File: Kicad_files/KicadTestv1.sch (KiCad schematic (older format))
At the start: 7 parts, among them J1 Conn_01x10_MountingPin, J2 Conn_01x04, SW1 SW_Push

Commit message: Ajout Lib pour RN2483 & Modificition Empreinte et cablage
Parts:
- removed J1: Conn_01x10_MountingPin, Connector_PinHeader_2.00mm:PinHeader_1x10_P2.00mm_Vertical, symbol Connector_Generic_MountingPin:Conn_01x10_MountingPin
- added U1: RN2483A, Socket_Arduino_Uno:Socket_Strip_Arduino_1x08, symbol Shield_Arduino:RN2483A
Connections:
- net labels added: +3V3
- wire segments 29 -> 34
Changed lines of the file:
@@
 	3450 2450 3450 2550
-$Comp
-L Connector_Generic_MountingPin:Conn_01x10_MountingPin J1
-U 1 1 5DDC7E9D
-P 5750 3800
-F 0 "J1" H 5838 3714 50  0000 L CNN
-F 1 "Conn_01x10_MountingPin" H 5838 3623 50  0000 L CNN
-F 2 "Connector_PinHeader_2.00mm:PinHeader_1x10_P2.00mm_Vertical" H 5750 3800 50  0001 C CNN
-F 3 "~" H 5750 3800 50  0001 C CNN
-	1    5750 3800
-	1    0    0    -1
-$EndComp
 $Comp
 L Connector_Generic:Conn_01x04 J2
@@
 Text GLabel 5300 3500 0    50   Input ~ 0
 Rx
-Text GLabel 5300 4000 0    50   Input ~ 0
+Text GLabel 5300 3700 0    50   Input ~ 0
 RST
 Wire Wire Line
@@
 Wire Wire Line
 	5300 3500 5550 3500
-Wire Wire Line
-	5550 4000 5300 4000
 Text GLabel 2350 4200 0    50   Input ~ 0
 Tx
@@
 	3250 4950 3250 4800
 Wire Wire Line
-	4700 3150 4700 4300
-Wire Wire Line
-	4700 4300 5550 4300
-Wire Wire Line
-	4700 4950 4700 4300
-Connection ~ 4700 4300
-Wire Wire Line
-	4050 4200 4050 3050
-Wire Wire Line
 	4050 2550 3450 2550
-Wire Wire Line
-	4050 4200 5550 4200
 Connection ~ 3450 2550
 Wire Wire Line
@@
 Wire Wire Line
 	4050 3050 4900 3050
-Connection ~ 4050 3050
 $Comp
 L Switch:SW_Push SW1
@@
 Wire Wire Line
 	2750 4000 2350 4000
+$Comp
+L Shield_Arduino:RN2483A U1
+U 1 1 5DE7C31C
+P 5750 3750
+F 0 "U1" V 5704 3978 50  0000 L CNN
+F 1 "RN2483A" V 5795 3978 50  0000 L CNN
+F 2 "Socket_Arduino_Uno:Socket_Strip_Arduino_1x08" H 6100 3700 50  0001 C CNN
+F 3 "" H 6100 3700 50  0001 C CNN
+	1    5750 3750
+	0    1    1    0
+$EndComp
+Wire Wire Line
+	4700 3150 4700 4100
+Wire Wire Line
+	5550 4100 4700 4100
+Connection ~ 4700 4100
+Wire Wire Line
+	4700 4100 4700 4950
+Wire Wire Line
+	5550 3700 5300 3700
+$Comp
+L power:+3V3 #PWR0101
+U 1 1 5DE826CD
+P 3300 2450
+F 0 "#PWR0101" H 3300 2300 50  0001 C CNN
+F 1 "+3V3" H 3315 2623 50  0000 C CNN
+F 2 "" H 3300 2450 50  0001 C CNN
+F 3 "" H 3300 2450 50  0001 C CNN
+	1    3300 2450
+	1    0    0    -1
+$EndComp
+Wire Wire Line
+	3300 2450 3300 2700
+Wire Wire Line
+	3300 2700 3350 2700
+$Comp
+L power:+3V3 #PWR0102
+U 1 1 5DE833AF
+P 4950 3850
+F 0 "#PWR0102" H 4950 3700 50  0001 C CNN
+F 1 "+3V3" H 4965 4023 50  0000 C CNN
+F 2 "" H 4950 3850 50  0001 C CNN
+F 3 "" H 4950 3850 50  0001 C CNN
+	1    4950 3850
+	1    0    0    -1
+$EndComp
+Wire Wire Line
+	5550 3900 4950 3900
+Wire Wire Line
+	4950 3900 4950 3850
+Wire Wire Line
+	5550 4000 4950 4000
+Wire Wire Line
+	4950 4000 4950 3900
+Connection ~ 4950 3900
+Text GLabel 4050 3700 2    50   Input ~ 0
+A0
+Wire Wire Line
+	4050 3700 3750 3700
 $EndSCHEMATC

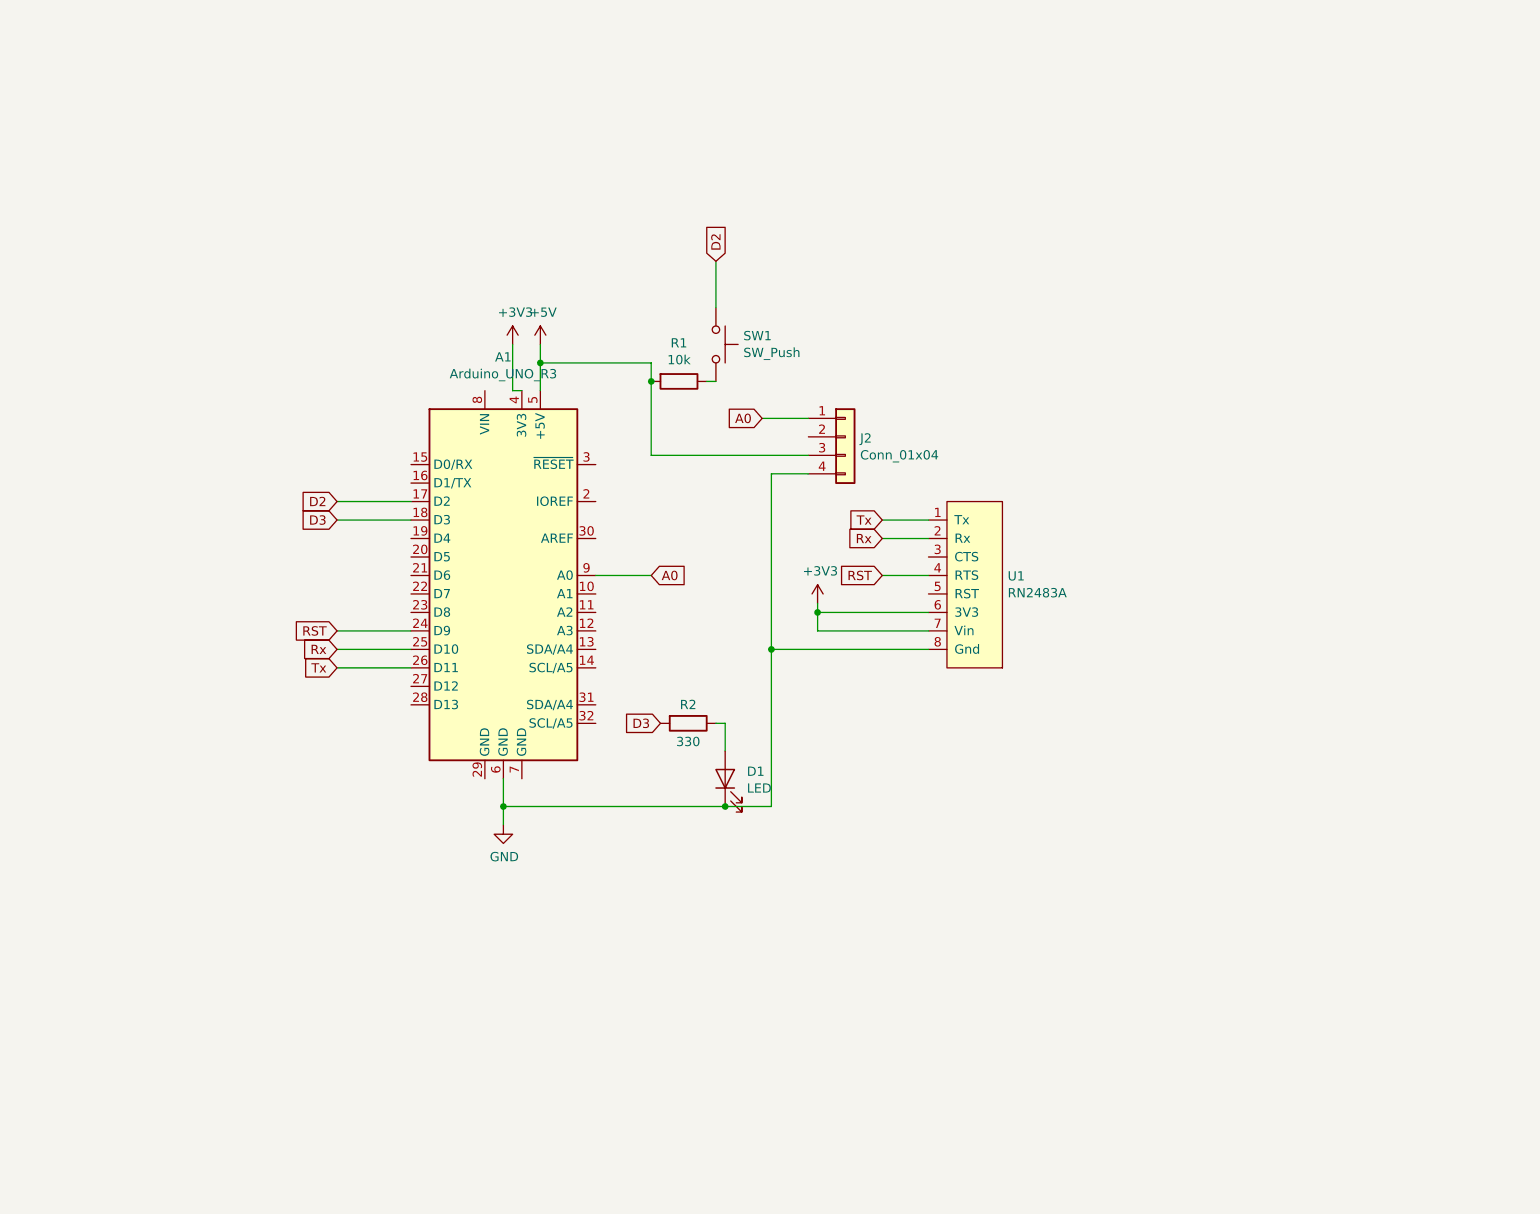
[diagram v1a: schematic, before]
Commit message: Modification empreinte et ajout circuit capteur AIME + faire routage
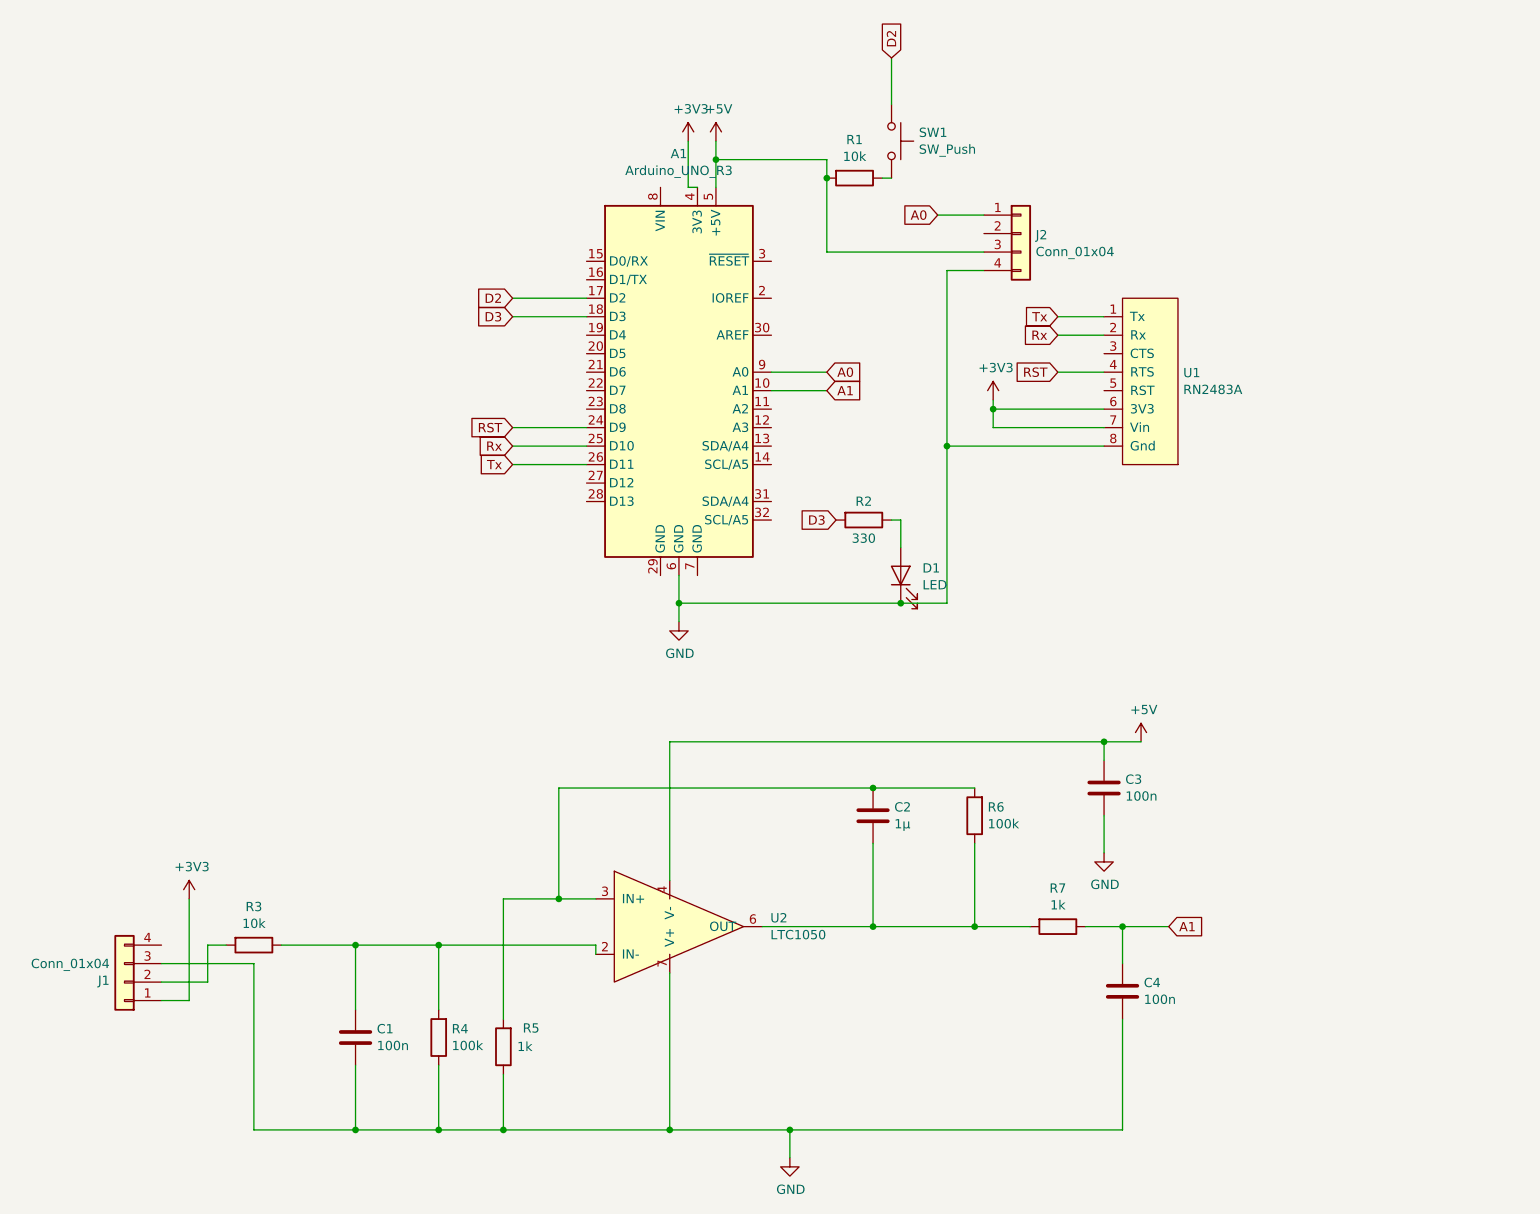
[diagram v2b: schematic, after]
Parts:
- added C1, C3, C4: 100n, Capacitor_THT:C_Axial_L3.8mm_D2.6mm_P7.50mm_Horizontal, symbol Device:C
- added C2: 1µ, Capacitor_THT:C_Rect_L7.0mm_W4.5mm_P5.00mm, symbol Device:C
- added J1: Conn_01x04, ShieldArduino_Empreintes:TO-5-4_1, symbol Connector_Generic:Conn_01x04
- added R3: 10k, Resistor_THT:R_Axial_DIN0204_L3.6mm_D1.6mm_P7.62mm_Horizontal, symbol Device:R
- added R4, R6: 100k, Resistor_THT:R_Axial_DIN0204_L3.6mm_D1.6mm_P7.62mm_Horizontal, symbol Device:R
- added R5, R7: 1k, Resistor_THT:R_Axial_DIN0204_L3.6mm_D1.6mm_P7.62mm_Horizontal, symbol Device:R
- added U2: LTC1050, symbol Shield_Arduino_suite:LTC1050
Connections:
- net +3V3: now also J1.1 (Pin_1)
- net +5V: now also C3.1, U2.4 (V-)
- net GND: now also C1.2, C3.2, C4.2, J1.3 (Pin_3), R4.1, R5.1, U2.7 (V+)
- net A1: now reaches A1.10 (A1)
- net A1: now also C4.1, R7.1
- new net: C2.2, R6.1, R7.2, U2.6 (OUT)
- new net: C1.1, R3.1, R4.2, U2.2 (IN-)
- new net: C2.1, R5.2, R6.2, U2.3 (IN+)
- new net: J1.2 (Pin_2), R3.2
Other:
- moved on the sheet: A1, D1, J2, R1, R2, SW1, U1

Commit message: Debut cablages
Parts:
- U2: footprint (none) -> Package_DIP:DIP-8_W7.62mm_LongPads
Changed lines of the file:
@@
 F 0 "U2" H 4694 5646 50  0000 L CNN
 F 1 "LTC1050" H 4694 5555 50  0000 L CNN
-F 2 "" H 4100 5600 50  0001 C CNN
+F 2 "Package_DIP:DIP-8_W7.62mm_LongPads" H 4100 5600 50  0001 C CNN
 F 3 "" H 4100 5600 50  0001 C CNN
 	1    4100 5600

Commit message: Cablage fait + verifier prochain commit si le module LoRa rentre
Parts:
- R1: footprint Resistor_THT:R_Axial_DIN0207_L6.3mm_D2.5mm_P10.16mm_Horizontal -> Resistor_THT:R_Axial_DIN0204_L3.6mm_D1.6mm_P7.62mm_Horizontal
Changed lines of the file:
@@
 F 0 "R1" V 4943 1550 50  0000 C CNN
 F 1 "10k" V 5034 1550 50  0000 C CNN
-F 2 "Resistor_THT:R_Axial_DIN0207_L6.3mm_D2.5mm_P10.16mm_Horizontal" V 5080 1550 50  0001 C CNN
+F 2 "Resistor_THT:R_Axial_DIN0204_L3.6mm_D1.6mm_P7.62mm_Horizontal" V 5080 1550 50  0001 C CNN
 F 3 "~" H 5150 1550 50  0001 C CNN
 	1    5150 1550

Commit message: Ajout de README + dossier pour image du README
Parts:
- A1: symbol MCU_Module:Arduino_UNO_R3 -> KicadTestv1-rescue:Arduino_UNO_R3-MCU_Module
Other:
- moved on the sheet: C1, C2, C3, C4, J1, R3, R4, R5, R6, R7, U2
